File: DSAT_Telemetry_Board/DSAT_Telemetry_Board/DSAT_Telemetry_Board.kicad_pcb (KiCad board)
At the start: 4 copper layers, 152.7 x 108.5 mm, 96 parts, among them IC1 CG2409X3-C2, J1 Conn_01x04_Female, J2 Conn_Coaxial, J3 Conn_01x02_Female, J5 Conn_01x04_Male, SW1 SW_Push, SW2 SW_SPDT, U1 AMS1117-3.3, U2 AMS1117-3.3, U3 AMS1117-3.3, U4 AMS1117-3.3, U5 STM32L433RCTx, U6 Si4463, U7 PSA4-5043+, U8 Watchdog_Timer, Y1 16MHz, Y2 30MHz

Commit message: Layout halfway done
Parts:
- moved D3 106.9 mm to (249.8, 151.8), turned to 0 degrees
- moved R4 106.6 mm to (252.6, 151.0), turned to 180 degrees
- moved C4 105.4 mm to (253.8, 149.6), turned to 0 degrees
- moved R9 105.1 mm to (166.0, 62.8)
- moved R7 104.0 mm to (249.4, 150.0), turned to 90 degrees
- moved C8 102.2 mm to (250.1, 148.5), turned to 0 degrees
- moved U4 96.8 mm to (251.8, 143.6), turned to 90 degrees
- moved C2 93.8 mm to (254.7, 118.4), turned to 0 degrees
- moved R2 93.7 mm to (253.3, 119.9), turned to 180 degrees
- moved D1 92.7 mm to (250.8, 121.9), turned to 0 degrees
- moved R5 90.1 mm to (250.3, 120.2), turned to 90 degrees
- moved C6 89.2 mm to (251.0, 118.4), turned to 0 degrees
- moved U2 87.2 mm to (252.9, 113.5), turned to 90 degrees
- moved D2 85.7 mm to (251.0, 136.8), turned to 0 degrees
- moved R3 84.9 mm to (253.4, 135.1), turned to 180 degrees
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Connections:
- R9 pad 2: /Microcontroller/USB_D- -> /D-
- U5 pad 44: /Microcontroller/USB_D- -> /D-
- U5 pad 45: /Microcontroller/USB_D+ -> /D+
- USB1 pad 11: +3.3V -> VBUS
- USB1 pad 2: +3.3V -> VBUS
- USB1 pad 5: /Microcontroller/USB_D- -> /D-
- USB1 pad 6: /Microcontroller/USB_D+ -> /D+
- USB1 pad 7: /USBC to USB 2.2/USB_D- -> /D-
- USB1 pad 8: /USBC to USB 2.2/USB_D+ -> /D+
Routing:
- net /D-: track 0.00 -> 58.1 mm
- net /D+: track 0.00 -> 55.1 mm
- net VBUS: track 33.9 -> 84.9 mm
- net GND: track 79.8 -> 112.4 mm
- net Net-(R13-Pad1): track 0.00 -> 6.80 mm
- net Net-(R12-Pad2): track 0.00 -> 5.34 mm
- net Net-(C7-Pad2): track 11.7 -> 8.71 mm
- net Net-(C6-Pad2): track 11.5 -> 8.92 mm
- net Net-(C8-Pad2): track 11.0 -> 8.63 mm
- net Net-(C5-Pad2): track 18.6 -> 17.6 mm
- net /Microcontroller/NRST: track 14.8 -> 15.6 mm
- net Net-(D2-Pad1): track 1.84 -> 1.16 mm
- net Net-(D1-Pad1): track 1.85 -> 1.25 mm
- net Net-(D3-Pad1): track 1.81 -> 1.21 mm
- net Net-(D4-Pad1): track 1.32 -> 0.76 mm
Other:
- board size 152.7 x 108.5 mm -> 152.7 x 108.6 mm

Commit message: Layout changes
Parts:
- added C34: 100nF, Capacitor_SMD:C_0402_1005Metric_Pad0.74x0.62mm_HandSolder, F.Cu at (180.0, 91.0)
- added C35: 100nF, Capacitor_SMD:C_0402_1005Metric_Pad0.74x0.62mm_HandSolder, F.Cu at (179.3, 89.0)
- moved R4 84.6 mm to (169.2, 136.6), turned to 90 degrees
- moved C4 83.9 mm to (170.7, 137.8), turned to -90 degrees
- moved D3 83.3 mm to (168.3, 134.4), turned to -90 degrees
- moved R7 80.9 mm to (170.2, 133.4), turned to 0 degrees
- moved C8 79.7 mm to (171.7, 134.1), turned to -90 degrees
- moved U4 75.5 mm to (176.7, 135.8), turned to 0 degrees
- moved R9 70.6 mm to (160.0, 133.1)
- moved R3 68.3 mm to (185.2, 137.5), turned to 90 degrees
- moved C3 67.7 mm to (187.2, 138.7), turned to -90 degrees
- moved D2 67.6 mm to (183.4, 135.1), turned to -90 degrees
- moved R6 65.3 mm to (185.2, 134.6), turned to 0 degrees
- moved C7 64.1 mm to (186.9, 135.1), turned to -90 degrees
- moved U3 61.5 mm to (192.0, 136.9), turned to 0 degrees
- moved TP18 60.2 mm to (218.7, 144.9), turned to 0 degrees
- moved C2 56.6 mm to (201.8, 138.8), turned to -90 degrees
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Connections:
- U5 pad 15: /Microcontroller/TX_SCK -> /TX_SCLK
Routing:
- net GND: track 112.4 -> 224.9 mm, vias 0 -> 55
- net /TX_SCLK: track 0.00 -> 46.7 mm
- net /TX_SDO: track 0.00 -> 35.2 mm
- net /TX_SDI: track 0.00 -> 33.9 mm, vias 0 -> 2
- net /TX_~{IRQ}: track 0.00 -> 32.6 mm
- net /TX_~{SEL}: track 0.00 -> 29.9 mm
- net /Microcontroller/DEBUG_CLK: track 0.00 -> 20.3 mm
- net /TX_En: track 0.00 -> 19.6 mm
- net /Microcontroller/DEBUG_DIO: track 0.00 -> 18.2 mm
- net /RX_En: track 0.00 -> 17.5 mm
- net Net-(C26-Pad1): track 0.00 -> 11.3 mm
- net /D+: track 55.1 -> 47.2 mm
- net /D-: track 58.1 -> 50.2 mm
- net Net-(C5-Pad2): track 17.6 -> 11.6 mm
- net Net-(C22-Pad1): track 1.36 -> 6.86 mm
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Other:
- board size 152.7 x 108.6 mm -> 95.4 x 104.3 mm

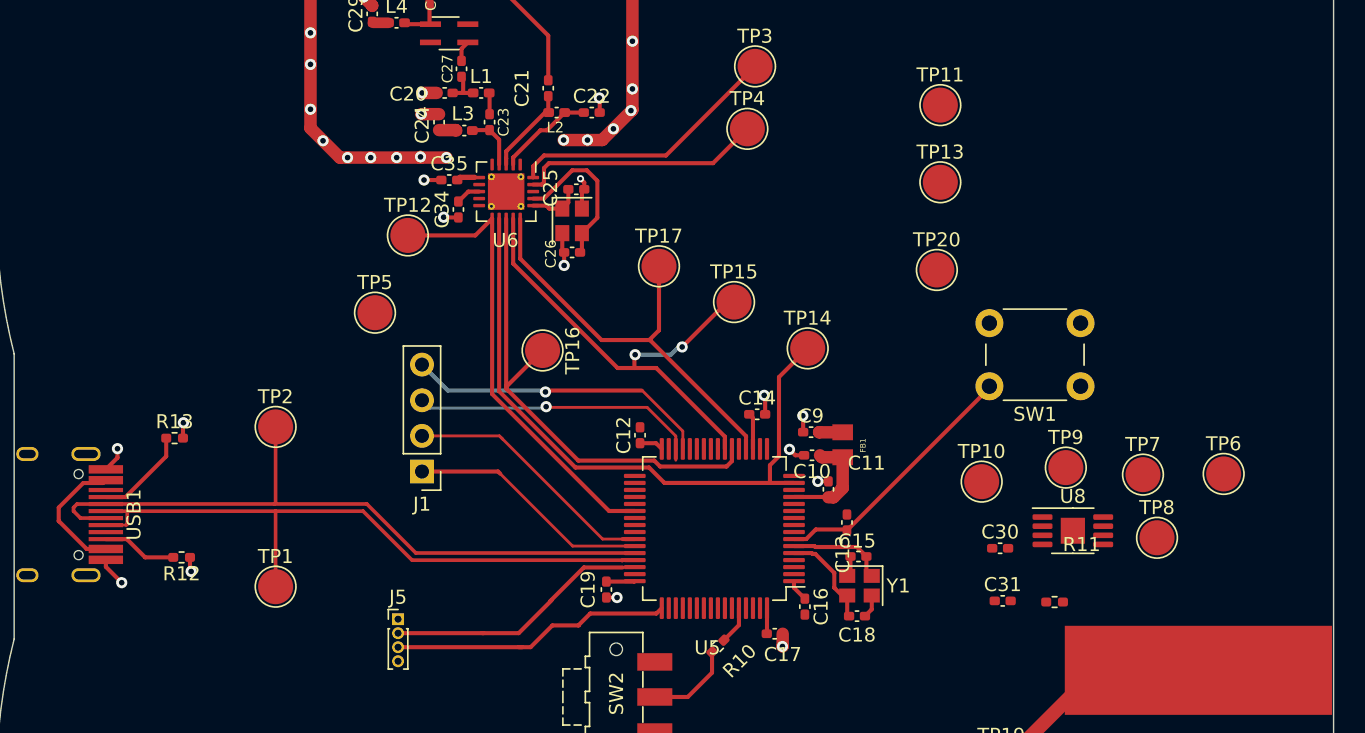
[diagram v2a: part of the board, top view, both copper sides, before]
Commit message: Added Watchdog Timer Footprint
Added custom footprint for watchdog timer
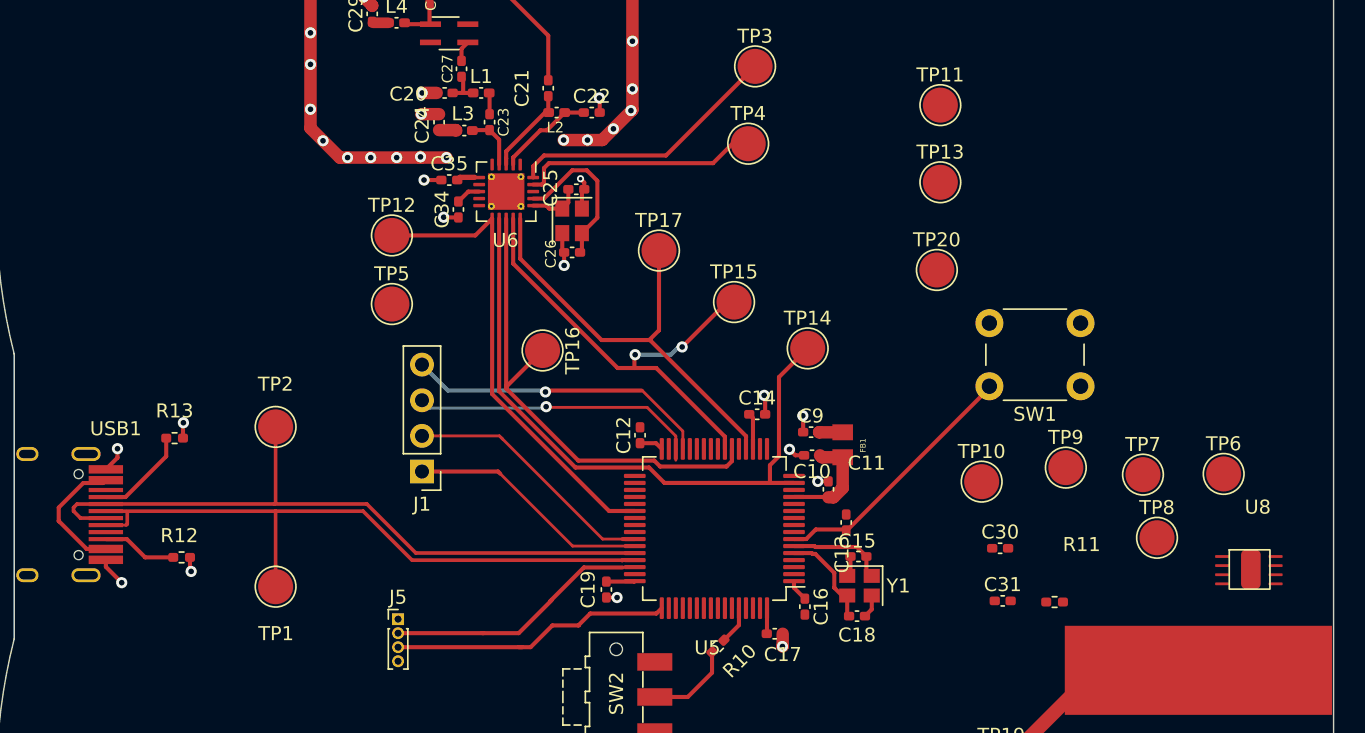
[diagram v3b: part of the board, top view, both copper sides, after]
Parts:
- U8: footprint Package_SO:MSOP-8-1EP_3x3mm_P0.65mm_EP1.73x1.85mm -> Watchdog_Footprints:Watchdog_Timer
- moved U8 11.9 mm to (234.9, 118.1)
- moved TP5 1.35 mm to (175.3, 97.8)
- moved TP12 1.14 mm to (175.3, 92.9)
- moved TP17 1.12 mm to (194.3, 94.0)
- moved TP4 1.06 mm to (200.7, 86.4)
- moved C13 0.05 mm to (207.6, 113.4)
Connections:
- U8 pad 1: (no net) -> /Watchdog_Timer/~{W}/T
- U8 pad 2: (no net) -> Net-(C30-Pad2)
- U8 pad 3: (no net) -> Net-(C31-Pad2)
- U8 pad 4: (no net) -> GND
- U8 pad 5: (no net) -> /WEN
- U8 pad 6: (no net) -> /~{WDO}
- U8 pad 7: (no net) -> /WDI
- U8 pad 8: (no net) -> +3V3
- U8 pad 9: (no net) -> GND
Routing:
- net Net-(C23-Pad1): track 5.51 -> 3.98 mm
- net /Transceiver1/TX_Transceiver: track 0.00 -> 1.53 mm

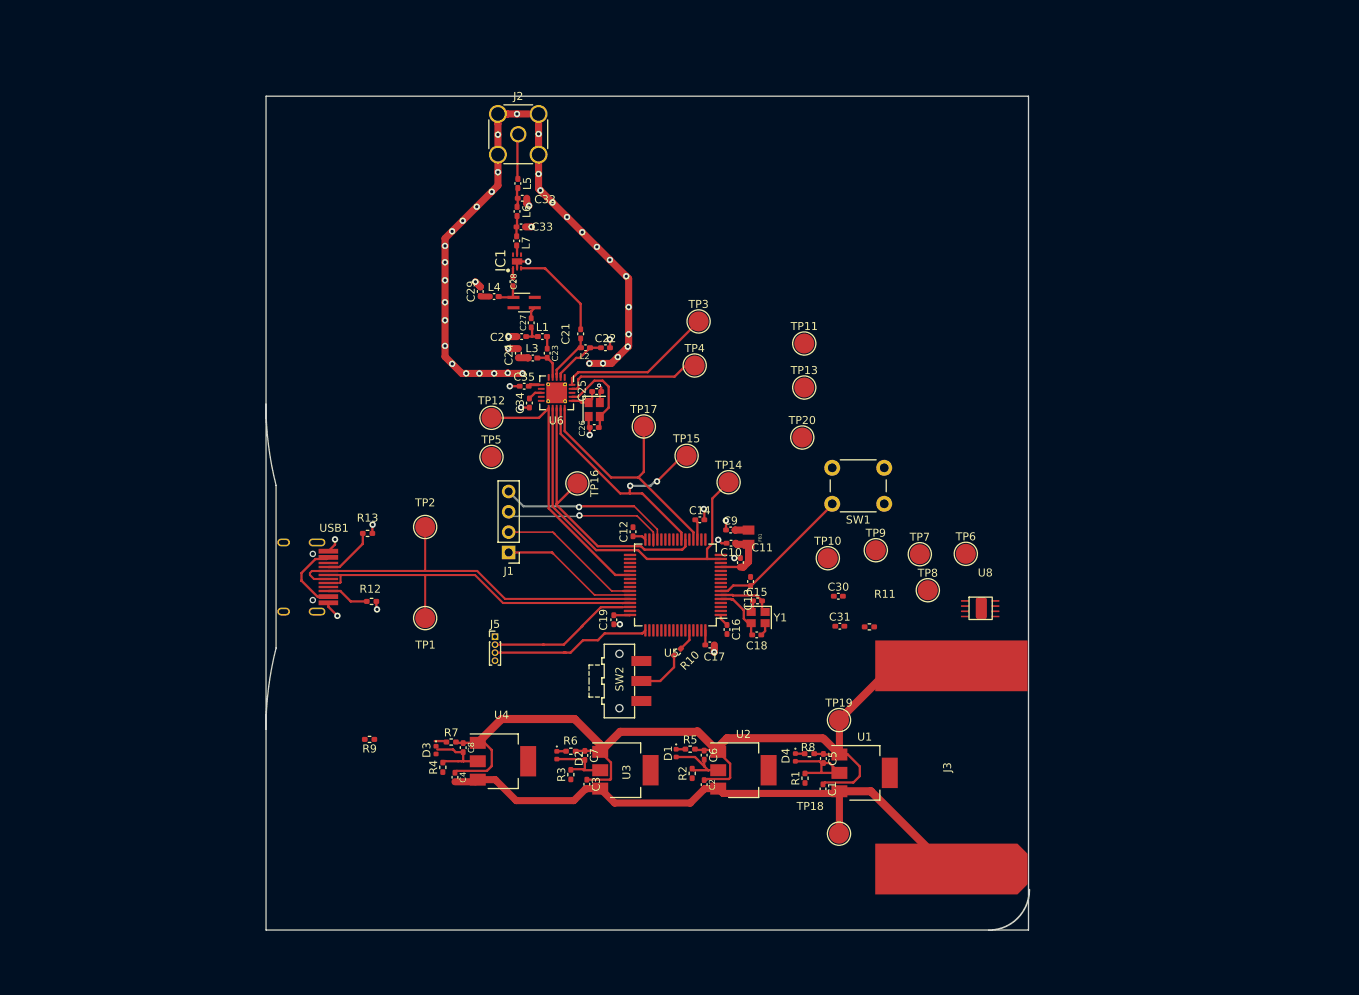
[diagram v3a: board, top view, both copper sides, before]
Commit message: Fixed PCB
Added new voltage regulator, reorganized everything, added new lines, fixed most DRC issues. Added ground and power pours. Added more vias.
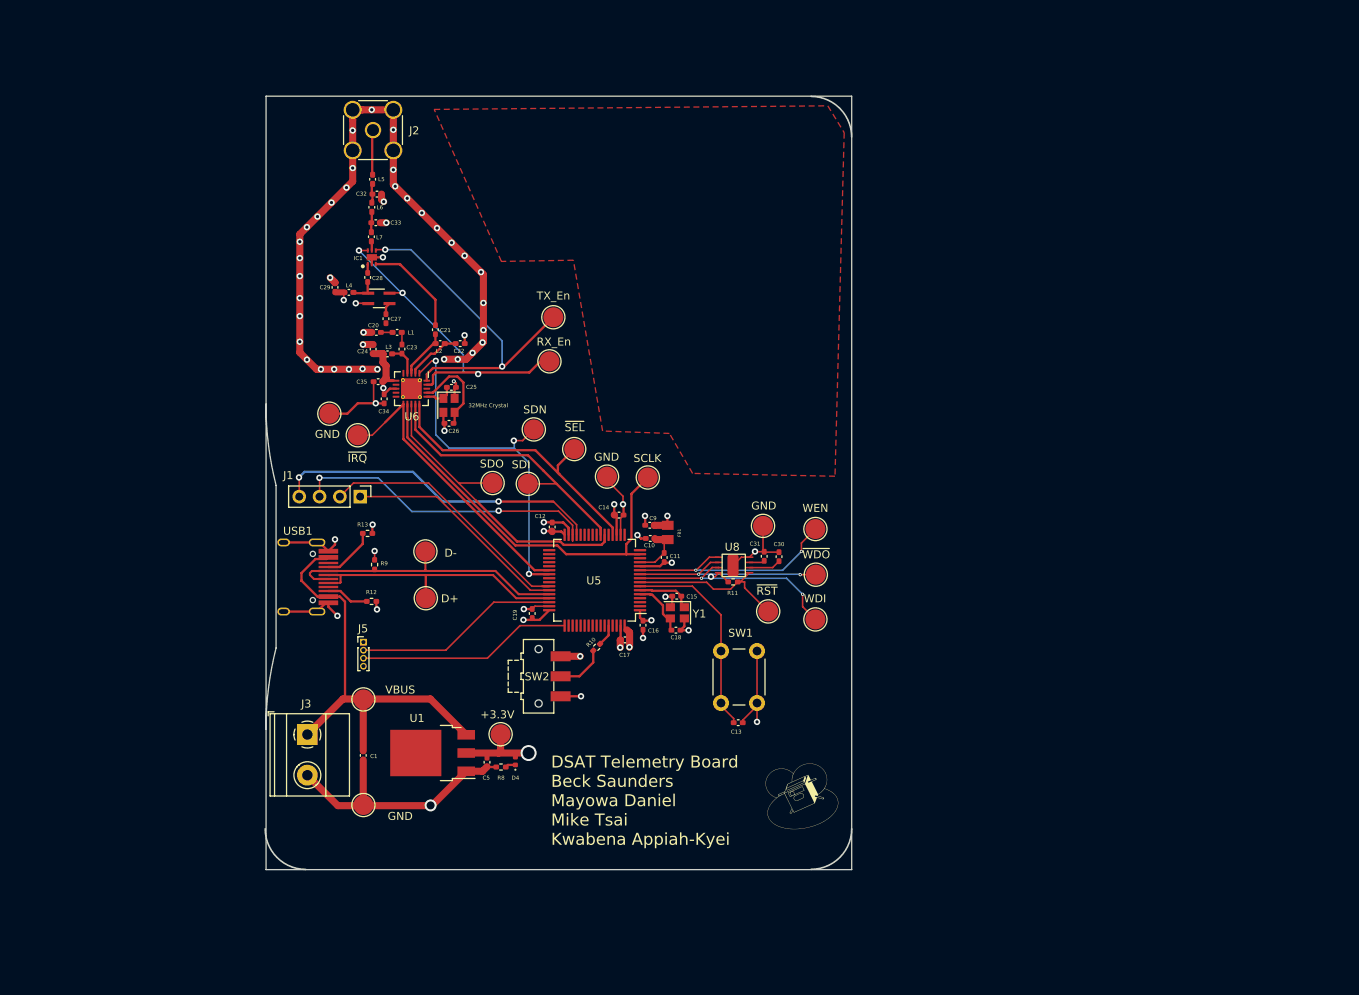
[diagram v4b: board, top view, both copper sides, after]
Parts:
- removed C2, C3, C4, C6, C7, C8: 22uF, Capacitor_SMD:C_0402_1005Metric_Pad0.74x0.62mm_HandSolder
- removed D1, D2, D3: LED, LED_SMD:LED_0402_1005Metric
- removed R1, R2, R3, R4: 10mOhm, Resistor_SMD:R_0402_1005Metric_Pad0.72x0.64mm_HandSolder
- removed R5, R6, R7: 1k5, Resistor_SMD:R_0402_1005Metric_Pad0.72x0.64mm_HandSolder
- removed U2, U3, U4: AMS1117-3.3, Package_TO_SOT_SMD:SOT-223-3_TabPin2
- added G***: LOGO, Watchdog_Footprints:Logo, F.Cu at (214.2, 140.2)
- J3: footprint Footprints:EDGE_PADS -> TerminalBlock_Phoenix:TerminalBlock_Phoenix_MKDS-1,5-2-5.08_1x02_P5.08mm_Horizontal
- U1: value AMS1117-3.3 -> AZ1084-3.3; footprint Package_TO_SOT_SMD:SOT-223-3_TabPin2 -> Package_TO_SOT_SMD:TO-252-3_TabPin2
- moved J3 80.6 mm to (152.2, 132.5), turned to -90 degrees
- moved VBUS 61.8 mm to (159.2, 128.1), turned to 180 degrees
- moved GND 60.4 mm to (159.2, 141.3), turned to 180 degrees
- moved C1 57.6 mm to (159.2, 135.1), turned to 90 degrees
- moved U1 54.1 mm to (167.9, 134.8), turned to 180 degrees
- moved +3.3V 52.9 mm to (176.4, 132.4)
- moved C5 42.1 mm to (174.7, 135.9), turned to 90 degrees
- moved R8 38.6 mm to (176.4, 136.6), turned to 180 degrees
- moved D4 35.0 mm to (178.2, 135.8), turned to 90 degrees
- moved SDN 34.2 mm to (180.6, 94.3)
- moved SW1 32.2 mm to (204.0, 128.6), turned to 90 degrees
- moved GND 29.7 mm to (189.7, 100.2)
- moved U8 29.1 mm to (207.0, 109.9), turned to 180 degrees
- moved GND 25.6 mm to (209.2, 106.4)
- moved R9 21.9 mm to (160.7, 111.2), turned to -90 degrees
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- renumbered TP20 to +3.3V, TP1 to D+, TP2 to D-, TP6 to GND, TP11 to GND, TP5 to GND, TP19 to GND, TP4 to RX_En, TP14 to SCLK, TP15 to SDI, TP13 to SDN, TP16 to SDO, TP3 to TX_En, TP18 to VBUS, TP9 to WDI, TP10 to WEN, TP12 to ~{IRQ}, TP7 to ~{RST}, TP17 to ~{SEL}, TP8 to ~{WDO}
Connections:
- +3.3V pad 1: Net-(C5-Pad2) -> +3.3V
- C5 pad 2: Net-(C5-Pad2) -> +3.3V
- D4 pad 2: Net-(C5-Pad2) -> +3.3V
- R11 pad 1: /Watchdog_Timer/~{W}/T -> /~{RST}
- R11 pad 2: +3V3 -> +3.3V
- U1 pad 2: Net-(C5-Pad2) -> +3.3V
- U5 pad 10: /WDI -> /~{WDO}
- U5 pad 33: /~{RST} -> unconnected-(U5-Pad33)
- U5 pad 34: /~{WDO} -> unconnected-(U5-Pad34)
- U5 pad 8: unconnected-(U5-Pad8) -> /~{RST}
- U5 pad 9: unconnected-(U5-Pad9) -> /WDI
- U8 pad 1: /Watchdog_Timer/~{W}/T -> /~{RST}
- U8 pad 8: +3V3 -> +3.3V
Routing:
- net /TX_SDN: track 0.00 -> 45.5 mm, vias 0 -> 3
- net VBUS: track 85.1 -> 54.1 mm
- net +3.3V: track 17.0 -> 47.4 mm, vias 0 -> 12
- net /WEN: track 0.00 -> 28.3 mm, vias 0 -> 2
- net /WDI: track 0.00 -> 27.8 mm, vias 0 -> 2
- net /~{WDO}: track 0.00 -> 25.1 mm, vias 0 -> 2
- net /TX_En: track 19.6 -> 43.3 mm, vias 0 -> 2
- net /RX_En: track 17.5 -> 41.2 mm, vias 0 -> 2
- net /~{RST}: track 0.00 -> 20.6 mm
- net /Microcontroller/I2C2_SCL: track 22.2 -> 41.7 mm, vias 1 -> 2
- net /Microcontroller/I2C2_SDA: track 21.0 -> 38.6 mm, vias 1 -> 2
- net /D+: track 47.2 -> 33.5 mm
- net /D-: track 50.2 -> 36.8 mm
- net /Microcontroller/I2C1_SCL: track 19.4 -> 32.2 mm
- net Net-(C5-Pad2): track 11.6 -> 0.00 mm
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- added copper zone on F.Cu, net (none)
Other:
- board size 95.4 x 104.3 mm -> 73.3 x 96.7 mm
- board text added: "32MHz Crystal"
- board text added: "DSAT Telemetry Board Beck Saunders Mayowa Daniel Mike Tsai Kwabena Appiah-Kyei"

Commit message: Layout should be doen
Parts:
- removed R9: 1k5, Resistor_SMD:R_0402_1005Metric_Pad0.72x0.64mm_HandSolder
- moved C26 4.24 mm to (173.7, 91.5), turned to -90 degrees
- moved C25 2.41 mm to (169.2, 91.2), turned to -90 degrees
- moved Y2 1.48 mm to (171.4, 91.5), turned to 0 degrees
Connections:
- C27 pad 1: /Low Noise Amplifier1/TX_Transciever -> /Transceiver1/TX_Transceiver
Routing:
- net Net-(C26-Pad1): track 11.3 -> 7.35 mm
- net /TX_SDN: track 45.5 -> 42.2 mm
- net GND: track 217.1 -> 218.6 mm, vias 64 -> 65
- net /Transceiver1/TX_Transceiver: track 1.46 -> 2.87 mm
- net +3.3V: track 47.4 -> 46.3 mm, vias 12 -> 11
- net /RX_En: track 41.2 -> 40.2 mm
- net Net-(C25-Pad2): track 3.72 -> 4.62 mm
- net (no net): vias 0 -> 173
- added copper zone on F.Cu, net GND
- removed copper zone on F.Cu, net (none)

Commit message: Layout should be doen
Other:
- board size 73.3 x 96.7 mm -> 73.2 x 96.7 mm
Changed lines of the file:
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@@
   (gr_arc (start 148.336 101.346) (mid 147.384731 96.305534) (end 147.066 91.186) (layer "Edge.Cuts") (width 0.1))
   (gr_rect (start 147.081781 149.376) (end 220.286 52.696) (layer "Edge.Cuts") (width 0.1) (fill none))
+  (gr_arc (start 147.102102 58.202102) (mid 148.566569 54.459626) (end 152.182102 52.705) (layer "Edge.Cuts") (width 0.2))
   (gr_line (start 148.336 101.346) (end 148.336 121.666) (layer "Edge.Cuts") (width 0.1))
   (gr_arc (start 220.287898 144.257898) (mid 218.8 147.85) (end 215.207898 149.337898) (layer "Edge.Cuts") (width 0.2))
-  (gr_arc (start 152.05 149.35) (mid 148.457898 147.862102) (end 146.97 144.27) (layer "Edge.Cuts") (width 0.2))
+  (gr_arc (start 152.05 149.35) (mid 148.581887 147.946488) (end 147.066 144.526) (layer "Edge.Cuts") (width 0.2))
   (gr_arc (start 147.066 131.826) (mid 147.384731 126.706466) (end 148.336 121.666) (layer "Edge.Cuts") (width 0.1))
   (gr_text "32MHz Crystal\n" (at 171.96106 86.442294 90) (layer "F.SilkS")
@@
     (connect_pads (clearance 0))
     (min_thickness 0.254) (filled_areas_thickness no)
-    (fill yes (thermal_gap 0.508) (thermal_bridge_width 0.508))
+    (fill (thermal_gap 0.508) (thermal_bridge_width 0.508))
     (polygon
       (pts
@@
     (connect_pads (clearance 0))
     (min_thickness 0.254) (filled_areas_thickness no)
-    (fill yes (thermal_gap 0.508) (thermal_bridge_width 0.508))
+    (fill (thermal_gap 0.508) (thermal_bridge_width 0.508))
     (polygon
       (pts
@@
     (connect_pads (clearance 0))
     (min_thickness 0.254) (filled_areas_thickness no)
-    (fill yes (thermal_gap 0.508) (thermal_bridge_width 0.508))
+    (fill (thermal_gap 0.508) (thermal_bridge_width 0.508))
     (polygon
       (pts
@@
     (connect_pads (clearance 0.508))
     (min_thickness 0.254) (filled_areas_thickness no)
-    (fill yes (thermal_gap 0.508) (thermal_bridge_width 0.508))
+    (fill (thermal_gap 0.508) (thermal_bridge_width 0.508))
     (polygon
       (pts
@@
     (connect_pads (clearance 0))
     (min_thickness 0.254) (filled_areas_thickness no)
-    (fill yes (thermal_gap 0.508) (thermal_bridge_width 0.508))
-    (polygon
-      (pts
+    (fill (thermal_gap 0.508) (thermal_bridge_width 0.508))
+    (polygon
+      (pts

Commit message: done
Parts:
- added C2: 1uF, Capacitor_SMD:C_0402_1005Metric_Pad0.74x0.62mm_HandSolder, F.Cu at (194.2, 123.8)
- added C3: 1uF, Capacitor_SMD:C_0402_1005Metric_Pad0.74x0.62mm_HandSolder, F.Cu at (170.9, 95.1)
- added C4: 100uF, Capacitor_THT:C_Axial_L3.8mm_D2.6mm_P7.50mm_Horizontal, F.Cu at (190.6, 130.5)
- renumbered D+ to TP1, WEN to TP10, GND to TP11, ~{IRQ} to TP12, SDN to TP13, SCLK to TP14, SDI to TP15, SDO to TP16, ~{SEL} to TP17, VBUS to TP18, GND to TP19, D- to TP2, +3.3V to TP20, TX_En to TP3, RX_En to TP4, GND to TP5, GND to TP6, ~{RST} to TP7, ~{WDO} to TP8, WDI to TP9
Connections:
- C27 pad 1: /Transceiver1/TX_Transceiver -> /Low Noise Amplifier1/TX_Transciever
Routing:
- net +3.3V: track 46.3 -> 48.4 mm, vias 11 -> 13
- net GND: track 218.6 -> 220.3 mm, vias 65 -> 67
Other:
- board size 73.2 x 96.7 mm -> 73.2 x 96.6 mm

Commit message: Fixed PCB Errors
Changed Design rules to allow certain clearance issues, changed keepout zone on STM32 Crystal, changed Footprint of Regulator
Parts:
- U1: footprint Package_TO_SOT_SMD:TO-252-3_TabPin2 -> Package_TO_SOT_SMD:TO-252-3_TabPin4
- moved GND 0.61 mm to (159.8, 141.2)
- renumbered TP20 to +3V3, TP1 to D+, TP2 to D-, TP6 to GND, TP11 to GND, TP5 to GND, TP19 to GND, TP4 to RX_En, TP3 to TX_En, TP14 to TX_SCLK, TP13 to TX_SDN, TP12 to TX_~{IRQ}, TP17 to TX_~{SEL}, TP18 to VBUS, TP9 to WDI, TP10 to WEN, TP7 to ~{RST}, TP8 to ~{WDO}
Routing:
- net GND: track 220.3 -> 224.3 mm, vias 67 -> 68
- net /Microcontroller/I2C2_SDA: track 38.6 -> 37.7 mm
